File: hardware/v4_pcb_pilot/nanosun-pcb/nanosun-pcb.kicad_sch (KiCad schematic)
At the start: 25 parts, among them J1 Conn_01x03

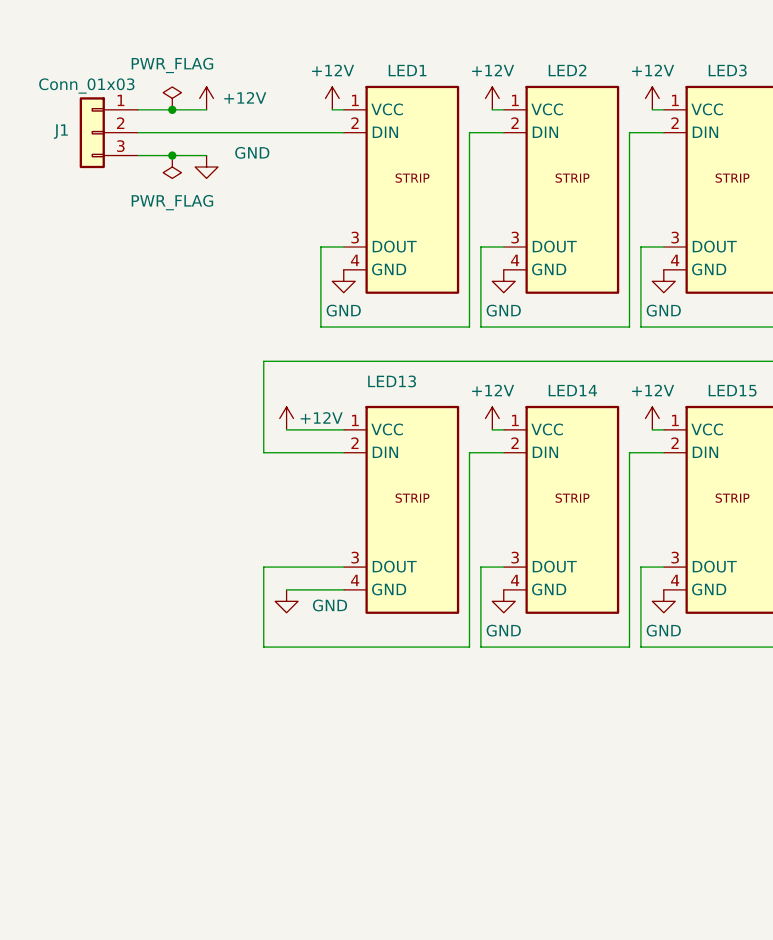
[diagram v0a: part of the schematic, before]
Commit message: fix pcb design issues
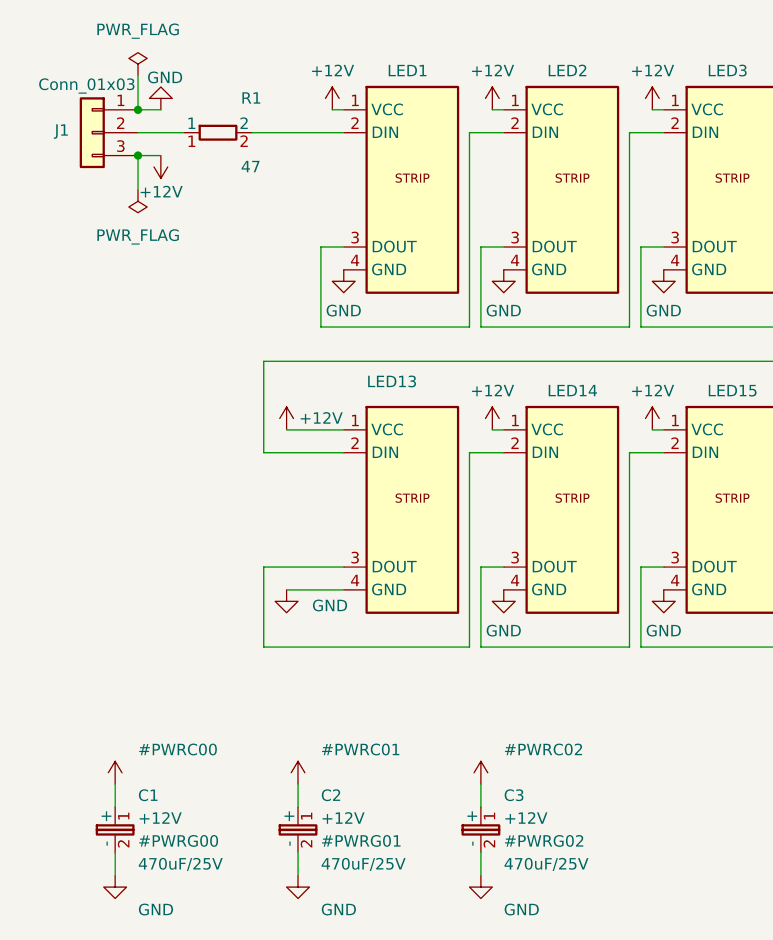
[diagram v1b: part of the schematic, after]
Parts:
- added C1, C2, C3: 470uF/25V, symbol nanosun-pcb:CP_THT
- added R1: 47, symbol nanosun-pcb:R_THT
- J1: footprint Connector_PinHeader_2.54mm:PinHeader_1x03_P2.54mm_Vertical -> TerminalBlock_Phoenix:TerminalBlock_Phoenix_MKDS-1,5-3_1x03_P5.00mm_Horizontal
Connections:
- net +12V: now also J1.3 (Pin_3), C1.1 (+), C2.1 (+), C3.1 (+); no longer J1.1 (Pin_1)
- net GND: now also J1.1 (Pin_1), C1.2 (-), C2.2 (-), C3.2 (-); no longer J1.3 (Pin_3)
- net at LED1.2 (DIN): now also R1.2; no longer J1.2 (Pin_2)
- new net: J1.2 (Pin_2), R1.1
